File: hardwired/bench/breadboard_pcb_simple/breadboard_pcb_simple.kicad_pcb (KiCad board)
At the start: 2 copper layers, 96.5 x 47 mm, 291 parts, among them J6 Conn_01x26_Pin, J7 Conn_01x26_Pin, J8 Conn_01x26_Pin

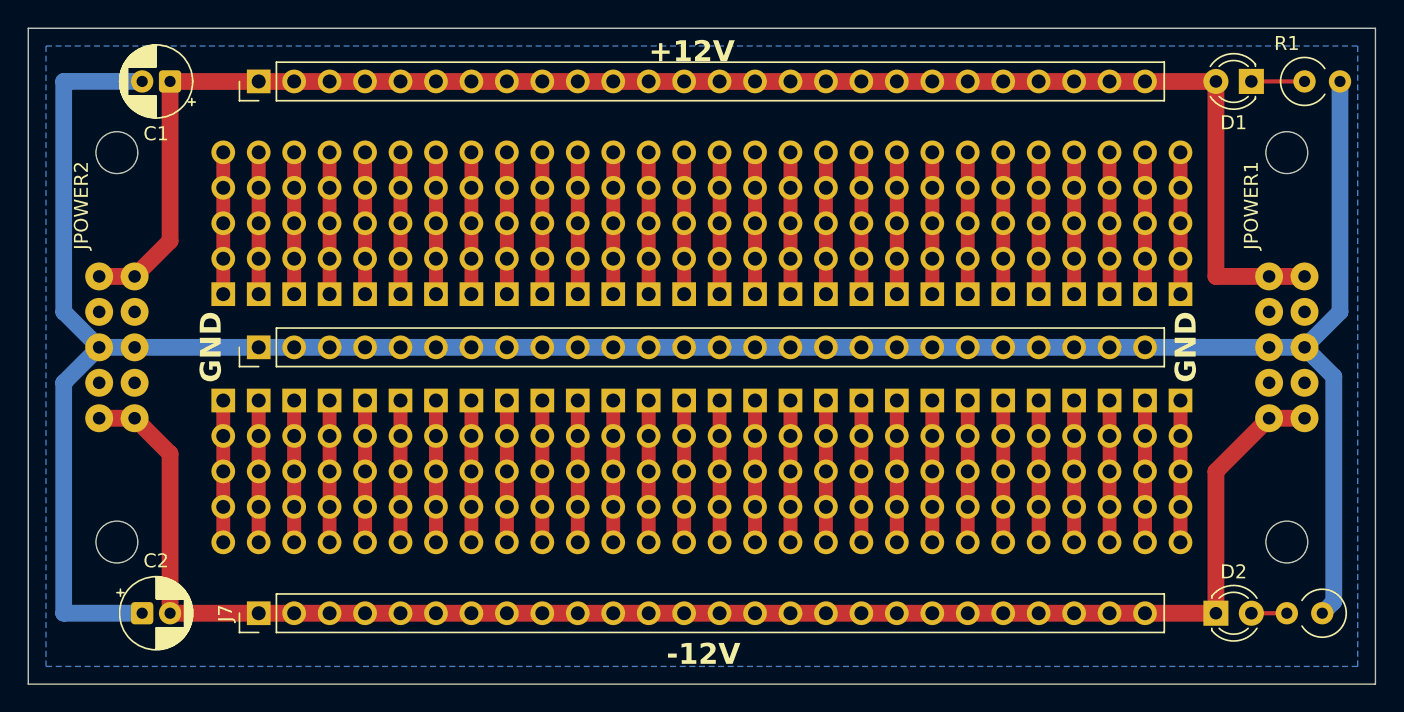
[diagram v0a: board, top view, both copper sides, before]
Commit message: Add improved breadboard PCB
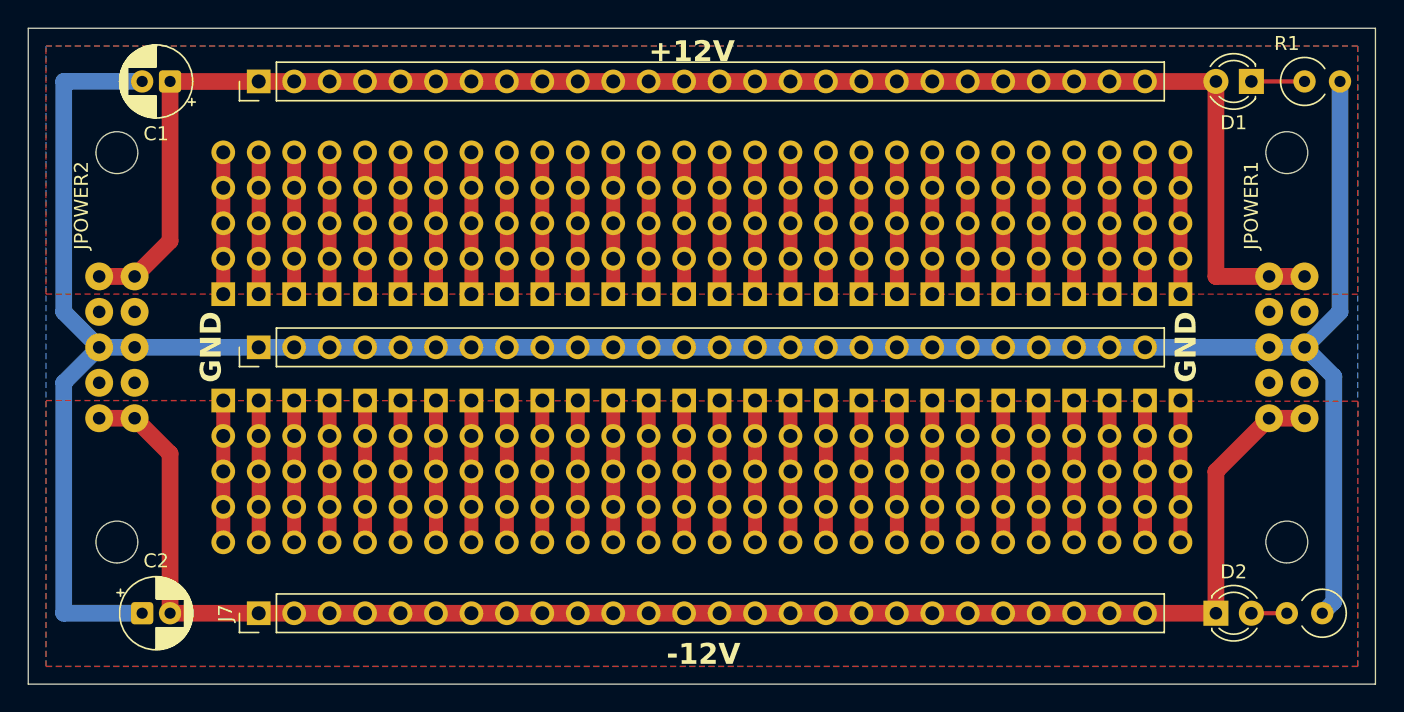
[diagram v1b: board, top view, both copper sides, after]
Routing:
- added copper zone on F.Cu, net +12V
- added copper zone on F.Cu, net -12V
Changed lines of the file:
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@@
+	)
+	(segment
+		(start 83.82 34.29)
+		(end 77.47 34.29)
+		(width 1.2)
+		(layer "F.Cu")
+		(net "+12V")
+	)
+	(segment
+		(start 74.93 48.26)
+		(end 72.39 48.26)
+		(width 1.2)
+		(layer "F.Cu")
+		(net "+12V")
+	)
+	(segment
+		(start 152.4 48.26)
+		(end 152.4 34.29)
+		(width 1.2)
+		(layer "F.Cu")
+		(net "+12V")
+	)
+	(segment
+		(start 158.75 48.26)
+		(end 152.4 48.26)
+		(width 1.2)
+		(layer "F.Cu")
+		(net "+12V")
+	)
+	(segment
+		(start 77.47 34.29)
+		(end 77.47 45.72)
+		(width 1.2)
+		(layer "F.Cu")
+		(net "+12V")
+	)
+	(segment
+		(start 152.4 34.29)
+		(end 83.82 34.29)
+		(width 1.2)
+		(layer "F.Cu")
+		(net "+12V")
+	)
+	(segment
+		(start 77.47 45.72)
+		(end 74.93 48.26)
+		(width 1.2)
+		(layer "F.Cu")
+		(net "+12V")
+	)
+	(segment
+		(start 158.75 48.26)
+		(end 156.21 48.26)
+		(width 1.2)
+		(layer "B.Cu")
+		(net "+12V")
 	)
 	(segment
@@
 	)
 	(segment
-		(start 83.82 34.29)
-		(end 77.47 34.29)
-		(width 1.2)
-		(layer "F.Cu")
-		(net "+12V")
-	)
-	(segment
-		(start 74.93 48.26)
-		(end 72.39 48.26)
-		(width 1.2)
-		(layer "F.Cu")
-		(net "+12V")
-	)
-	(segment
-		(start 152.4 48.26)
-		(end 152.4 34.29)
-		(width 1.2)
-		(layer "F.Cu")
-		(net "+12V")
-	)
-	(segment
-		(start 158.75 48.26)
-		(end 152.4 48.26)
-		(width 1.2)
-		(layer "F.Cu")
-		(net "+12V")
-	)
-	(segment
-		(start 77.47 34.29)
-		(end 77.47 45.72)
-		(width 1.2)
-		(layer "F.Cu")
-		(net "+12V")
-	)
-	(segment
-		(start 152.4 34.29)
-		(end 83.82 34.29)
-		(width 1.2)
-		(layer "F.Cu")
-		(net "+12V")
-	)
-	(segment
-		(start 77.47 45.72)
-		(end 74.93 48.26)
-		(width 1.2)
-		(layer "F.Cu")
-		(net "+12V")
-	)
-	(segment
-		(start 158.75 48.26)
-		(end 156.21 48.26)
-		(width 1.2)
-		(layer "B.Cu")
-		(net "+12V")
-	)
-	(segment
 		(start 75.47 72.39)
 		(end 69.85 72.39)
@@
 		(layer "B.Cu")
 		(net "GND")
+	)
+	(segment
+		(start 154.94 34.29)
+		(end 158.75 34.29)
+		(width 0.3)
+		(layer "F.Cu")
+		(net "Net-(D1-K)")
 	)
 	(segment
@@
 		(net "Net-(D2-A)")
 	)
-	(segment
-		(start 154.94 34.29)
-		(end 158.75 34.29)
-		(width 0.3)
-		(layer "F.Cu")
-		(net "Net-(D1-K)")
-	)
 	(zone
+		(net "-12V")
+		(layer "F.Cu")
+		(name "-12V")
+		(hatch edge 0.5)
+		(priority 2)
+		(connect_pads
+			(clearance 0.5)
+		)
+		(min_thickness 0.25)
+		(fill yes
+			(thermal_gap 0.5)
+			(thermal_bridge_width 0.5)
+			(island_removal_mode 0)
+		)
+		(polygon
+			(pts
+				(xy 162.56 76.2) (xy 68.58 76.2) (xy 68.58 57.15) (xy 162.570803 57.20345)
+			)
+		)
+	)
+	(zone
+		(net "+12V")
+		(layer "F.Cu")
+		(name "+12V")
+		(hatch edge 0.5)
+		(priority 1)
+		(connect_pads
+			(clearance 0.5)
+		)
+		(min_thickness 0.25)
+		(fill yes
+			(thermal_gap 0.5)
+			(thermal_bridge_width 0.5)
+			(island_removal_mode 0)
+		)
+		(polygon
+			(pts
+				(xy 68.58 31.75) (xy 162.56 31.75) (xy 162.56 49.53) (xy 68.579558 49.527665)
+			)
+		)
+	)
+	(zone
